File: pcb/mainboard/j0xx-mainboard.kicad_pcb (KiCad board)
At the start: 2 copper layers, 148 x 142 mm, 21 parts, among them J1 USB_C_Receptacle, Q1 BSS138, SW1 reset, U1 ATmega32U4-AU, Y1 Resonator

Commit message: wip
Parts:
- removed G***: LOGO, Outlines:pentagon
- added C7: 0.1u, Capacitor_SMD:C_0805_2012Metric, F.Cu at (237.4, 71.8)
- moved R5 43.6 mm to (240.2, 75.0), turned to 270 degrees
- moved C5 42.2 mm to (239.7, 82.2), turned to 270 degrees
- moved Y1 35.3 mm to (233.6, 88.1), turned to 180 degrees
- moved U1 34.1 mm to (234.0, 78.9), turned to 0 degrees
- moved C6 31.8 mm to (231.0, 72.6), turned to 0 degrees
- moved R7 29.2 mm to (228.5, 89.2), turned to 135 degrees
- moved SW1 27.0 mm to (226.3, 90.0), turned to 315 degrees
- moved C4 21.8 mm to (227.6, 75.3), turned to 90 degrees
- moved C3 19.0 mm to (223.2, 78.5), turned to 90 degrees
- moved C2 16.1 mm to (221.1, 78.5), turned to 90 degrees
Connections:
- J1 pad A10: (no net) -> Net-(J1-PadA10)
- J1 pad A3: (no net) -> Net-(J1-PadA3)
- J1 pad A8: (no net) -> Net-(J1-PadA8)
- J1 pad B10: (no net) -> Net-(J1-PadB10)
- J1 pad B3: (no net) -> Net-(J1-PadB3)
- J1 pad B8: (no net) -> Net-(J1-PadB8)
- U1 pad 1: (no net) -> BTN_MS
- U1 pad 10: (no net) -> BTN_LEFT
- U1 pad 11: (no net) -> BTN_DOWN
- U1 pad 12: (no net) -> BTN_RIGHT
- U1 pad 18: (no net) -> BTN_MODX
- U1 pad 19: (no net) -> BTN_MODY
- U1 pad 20: (no net) -> BTN_START
- U1 pad 21: (no net) -> Net-(U1-Pad21)
- U1 pad 22: (no net) -> Net-(U1-Pad22)
- U1 pad 25: (no net) -> Net-(U1-Pad25)
- U1 pad 26: (no net) -> Net-(U1-Pad26)
- U1 pad 27: (no net) -> BTN_CL
- U1 pad 28: (no net) -> BTN_CU
- U1 pad 29: (no net) -> BTN_CD
- U1 pad 30: (no net) -> BTN_A
- U1 pad 31: (no net) -> BTN_CR
- U1 pad 32: (no net) -> BTN_B
- U1 pad 36: (no net) -> BTN_X
- U1 pad 37: (no net) -> BTN_Z
- U1 pad 38: (no net) -> BTN_UP
- U1 pad 39: (no net) -> BTN_R
- U1 pad 40: (no net) -> BTN_Y
- U1 pad 41: (no net) -> BTN_LS
- U1 pad 42: (no net) -> Net-(U1-Pad42)
- U1 pad 9: (no net) -> BTN_L
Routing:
- net (no net): track 205.3 -> 0.00 mm
- net +5V: track 150.2 -> 128.2 mm
- net BTN_L: track 0.00 -> 16.4 mm
- net BTN_LEFT: track 0.00 -> 15.4 mm
- net BTN_DOWN: track 0.00 -> 14.5 mm
- net BTN_START: track 0.00 -> 14.2 mm
- net BTN_RIGHT: track 0.00 -> 13.4 mm
- net Net-(R3-Pad1): track 24.9 -> 37.4 mm
- net Net-(R4-Pad1): track 24.3 -> 36.0 mm
- net BTN_UP: track 0.00 -> 11.5 mm
- net BTN_Z: track 0.00 -> 11.3 mm
- net BTN_X: track 0.00 -> 11.1 mm
- net GND: track 74.3 -> 64.6 mm, vias 11 -> 9
- net GCCD5v: track 39.5 -> 47.2 mm
- net BTN_R: track 0.00 -> 7.08 mm
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- added copper zone on B.Cu, net GND
- added copper zone on F.Cu, net GND
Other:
- board size 148 x 142 mm -> 136.8 x 59.1 mm

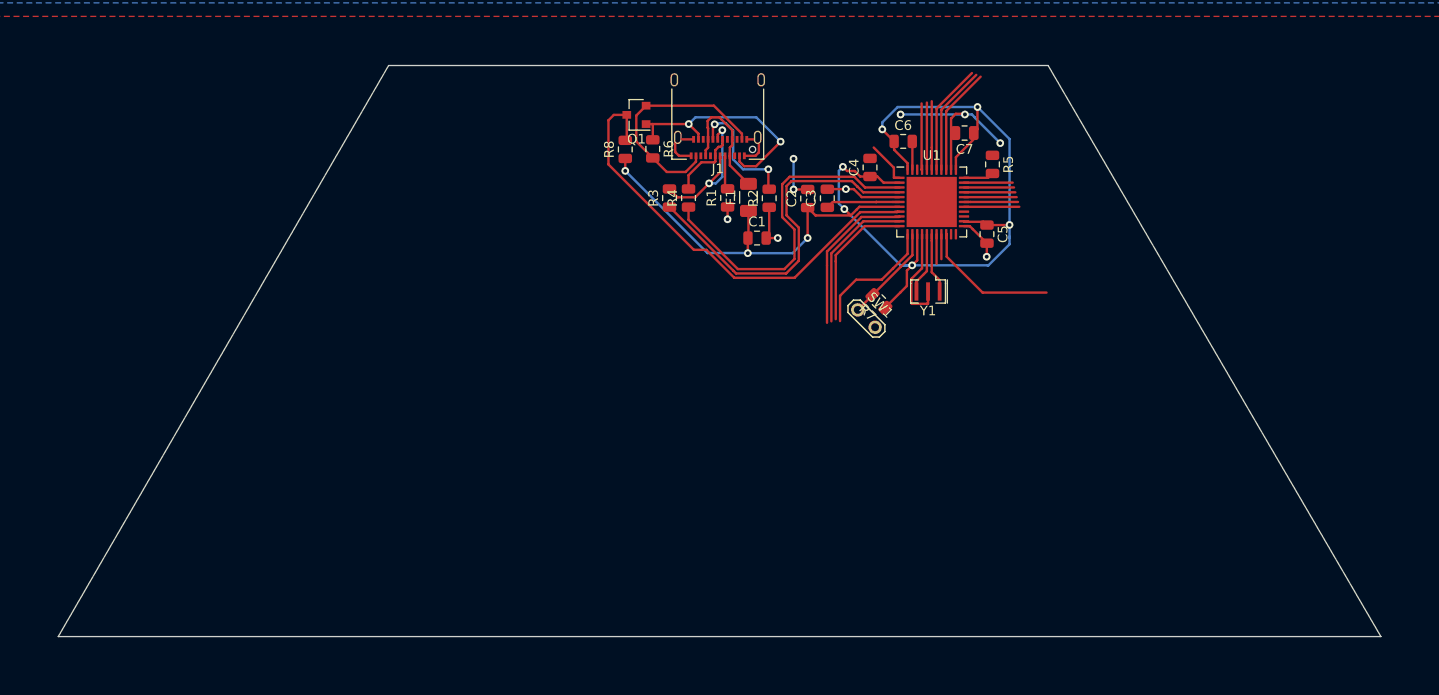
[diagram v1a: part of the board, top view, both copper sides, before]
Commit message: rearrange parts, add connectors and outline
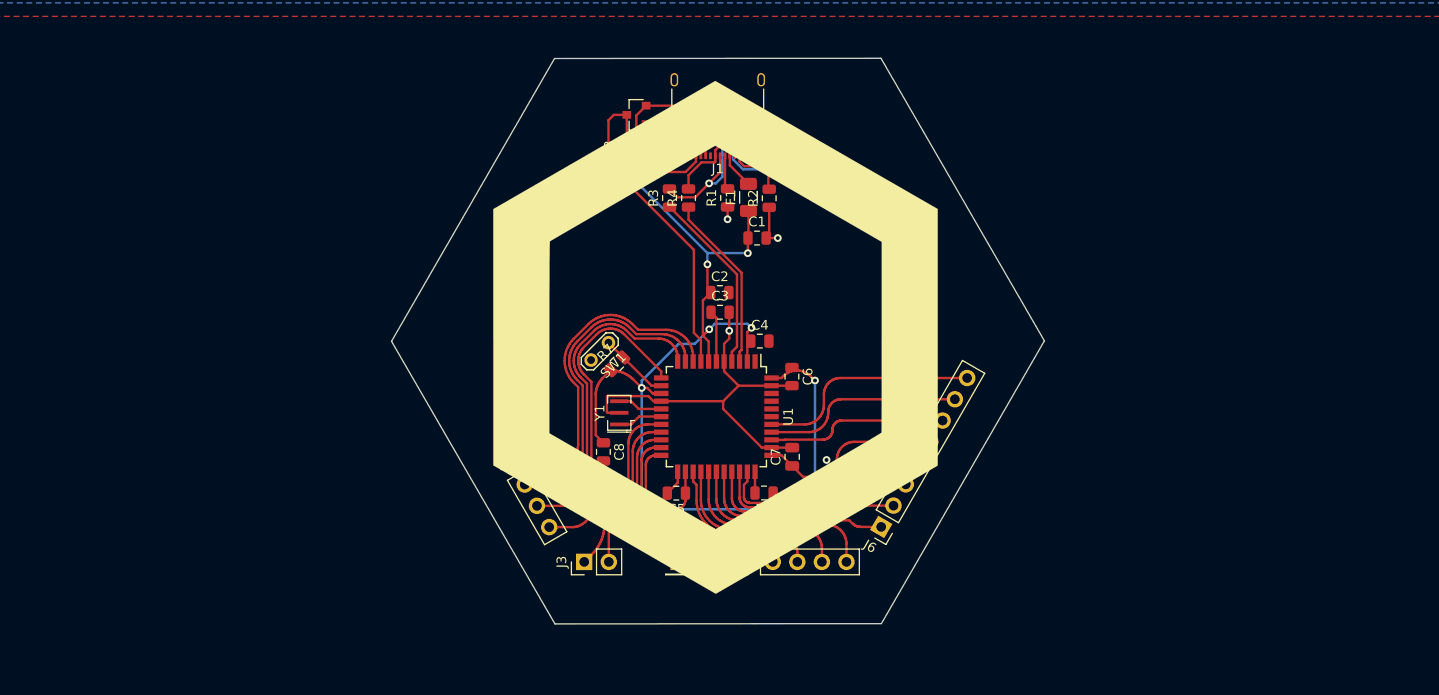
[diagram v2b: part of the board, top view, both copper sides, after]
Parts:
- added C8: 0.1u, Capacitor_SMD:C_0805_2012Metric, F.Cu at (200.0, 104.7)
- added G***: LOGO, Outlines:shine, F.Cu at (211.8, 92.8)
- added G***: LOGO, Outlines:shine, B.Cu at (211.8, 92.8)
- added J2: Conn_01x04, Connector_PinHeader_2.54mm:PinHeader_1x04_P2.54mm_Vertical, F.Cu at (190.6, 105.9)
- added J3: Conn_01x02, Connector_PinHeader_2.54mm:PinHeader_1x02_P2.54mm_Vertical, F.Cu at (198.0, 116.1)
- added J4: Conn_01x01, Connector_PinHeader_2.54mm:PinHeader_1x01_P2.54mm_Vertical, F.Cu at (207.8, 116.1)
- added J5: Conn_01x05, Connector_PinHeader_2.54mm:PinHeader_1x05_P2.54mm_Vertical, F.Cu at (215.0, 116.1)
- added J6: Conn_01x08, Connector_PinHeader_2.54mm:PinHeader_1x08_P2.54mm_Vertical, F.Cu at (228.7, 112.5)
- U1: footprint Package_DFN_QFN:QFN-44-1EP_7x7mm_P0.5mm_EP5.2x5.2mm -> Package_QFP:TQFP-44_10x10mm_P0.8mm
- moved C5 41.8 mm to (207.6, 109.0), turned to 180 degrees
- moved R5 41.4 mm to (216.6, 109.0), turned to 180 degrees
- moved C7 37.9 mm to (219.5, 105.2), turned to 90 degrees
- moved Y1 34.3 mm to (201.7, 100.7), turned to 90 degrees
- moved U1 31.4 mm to (211.7, 101.1), turned to 270 degrees
- moved R7 27.9 mm to (201.4, 95.6), turned to 45 degrees
- moved C6 26.9 mm to (219.5, 96.9), turned to 270 degrees
- moved SW1 26.0 mm to (200.5, 93.4), turned to 225 degrees
- moved C4 21.3 mm to (216.2, 93.3), turned to 0 degrees
- moved C3 16.2 mm to (212.1, 90.3), turned to 0 degrees
- moved C2 13.3 mm to (212.1, 88.3), turned to 0 degrees
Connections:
- U1 pad 1: BTN_MS -> Net-(U1-Pad1)
- U1 pad 21: Net-(U1-Pad21) -> BTN_CL
- U1 pad 22: Net-(U1-Pad22) -> BTN_CU
- U1 pad 25: Net-(U1-Pad25) -> BTN_CD
- U1 pad 26: Net-(U1-Pad26) -> BTN_A
- U1 pad 27: BTN_CL -> BTN_CR
- U1 pad 28: BTN_CU -> BTN_B
- U1 pad 29: BTN_CD -> BTN_X
- U1 pad 30: BTN_A -> BTN_Z
- U1 pad 31: BTN_CR -> BTN_UP
- U1 pad 32: BTN_B -> BTN_R
- U1 pad 36: BTN_X -> BTN_Y
- U1 pad 37: BTN_Z -> BTN_LS
- U1 pad 38: BTN_UP -> BTN_MS
- U1 pad 39: BTN_R -> Net-(U1-Pad39)
- U1 pad 40: BTN_Y -> Net-(U1-Pad40)
- U1 pad 41: BTN_LS -> Net-(U1-Pad41)
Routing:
- net BTN_RIGHT: track 13.4 -> 33.9 mm
- net BTN_R: track 7.08 -> 27.5 mm
- net BTN_DOWN: track 14.5 -> 34.5 mm
- net BTN_LEFT: track 15.4 -> 34.9 mm
- net BTN_L: track 16.4 -> 35.3 mm
- net BTN_MS: track 4.57 -> 23.4 mm
- net Net-(R3-Pad1): track 37.4 -> 19.1 mm
- net BTN_CU: track 5.58 -> 23.6 mm
- net Net-(R4-Pad1): track 36.0 -> 18.4 mm
- net BTN_CL: track 5.72 -> 22.4 mm
- net BTN_CR: track 5.17 -> 21.6 mm
- net BTN_B: track 5.04 -> 21.4 mm
- net BTN_MODX: track 3.06 -> 19.0 mm
- net BTN_MODY: track 2.57 -> 17.0 mm
- net BTN_A: track 5.31 -> 19.7 mm
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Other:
- board size 136.8 x 59.1 mm -> 67.5 x 58.5 mm

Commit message: wip
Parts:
- J2: value Conn_01x04 -> Conn_01x07; footprint Connector_PinHeader_2.54mm:PinHeader_1x04_P2.54mm_Vertical -> Connector_PinHeader_2.54mm:PinHeader_1x07_P2.54mm_Vertical
- J3: value Conn_01x02 -> Conn_01x05; footprint Connector_PinHeader_2.54mm:PinHeader_1x02_P2.54mm_Vertical -> Connector_PinHeader_2.54mm:PinHeader_1x05_P2.54mm_Vertical
- J4: value Conn_01x01 -> Conn_01x04; footprint Connector_PinHeader_2.54mm:PinHeader_1x01_P2.54mm_Vertical -> Connector_PinHeader_2.54mm:PinHeader_1x04_P2.54mm_Vertical
- J5: value Conn_01x05 -> Conn_01x08; footprint Connector_PinHeader_2.54mm:PinHeader_1x05_P2.54mm_Vertical -> Connector_PinHeader_2.54mm:PinHeader_1x08_P2.54mm_Vertical
- J6: value Conn_01x08 -> Conn_01x10; footprint Connector_PinHeader_2.54mm:PinHeader_1x08_P2.54mm_Vertical -> Connector_PinHeader_2.54mm:PinHeader_1x10_P2.54mm_Vertical
- moved J2 30.8 mm to (192.2, 75.2), turned to 330 degrees
- moved J6 24.6 mm to (240.7, 90.9), turned to 210 degrees
- moved J3 17.9 mm to (186.9, 102.1), turned to 30 degrees
- moved J5 15.1 mm to (229.9, 113.4), turned to 150 degrees
- moved J4 3.93 mm to (207.4, 120.0), turned to 90 degrees
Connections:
- J2 pad 1: BTN_L -> GND
- J2 pad 2: BTN_LEFT -> LED_DATA
- J2 pad 3: BTN_DOWN -> BTN_L
- J2 pad 4: BTN_RIGHT -> BTN_LEFT
- J3 pad 1: BTN_MODX -> GND
- J3 pad 2: BTN_MODY -> LED_1-2
- J4 pad 1: BTN_START -> GND
- J5 pad 1: BTN_CL -> GND
- J5 pad 2: BTN_CU -> LED_3-4
- J5 pad 3: BTN_CD -> BTN_CL
- J5 pad 4: BTN_A -> BTN_CU
- J5 pad 5: BTN_CR -> BTN_CD
- J6 pad 1: BTN_B -> GND
- J6 pad 2: BTN_X -> LED_4-5
- J6 pad 3: BTN_Z -> BTN_B
- J6 pad 4: BTN_UP -> BTN_X
- J6 pad 5: BTN_R -> BTN_Z
- J6 pad 6: BTN_Y -> BTN_UP
- J6 pad 7: BTN_LS -> BTN_R
- J6 pad 8: BTN_MS -> BTN_Y
- U1 pad 1: Net-(U1-Pad1) -> LED_DATA
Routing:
- net LED_DATA: track 0.00 -> 40.8 mm, vias 0 -> 2
- net LED_2-3: track 0.00 -> 30.0 mm
- net LED_3-4: track 0.00 -> 28.6 mm
- net BTN_B: track 21.4 -> 48.0 mm
- net BTN_X: track 21.8 -> 48.1 mm
- net LED_1-2: track 0.00 -> 25.4 mm
- net BTN_Z: track 23.3 -> 48.2 mm
- net BTN_UP: track 25.2 -> 48.3 mm
- net BTN_R: track 27.5 -> 48.9 mm
- net BTN_CL: track 22.4 -> 43.7 mm
- net BTN_CU: track 23.6 -> 44.8 mm
- net BTN_CD: track 17.6 -> 38.6 mm
- net BTN_A: track 19.7 -> 40.6 mm
- net BTN_CR: track 21.6 -> 42.4 mm
- net LED_4-5: track 0.00 -> 19.1 mm
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
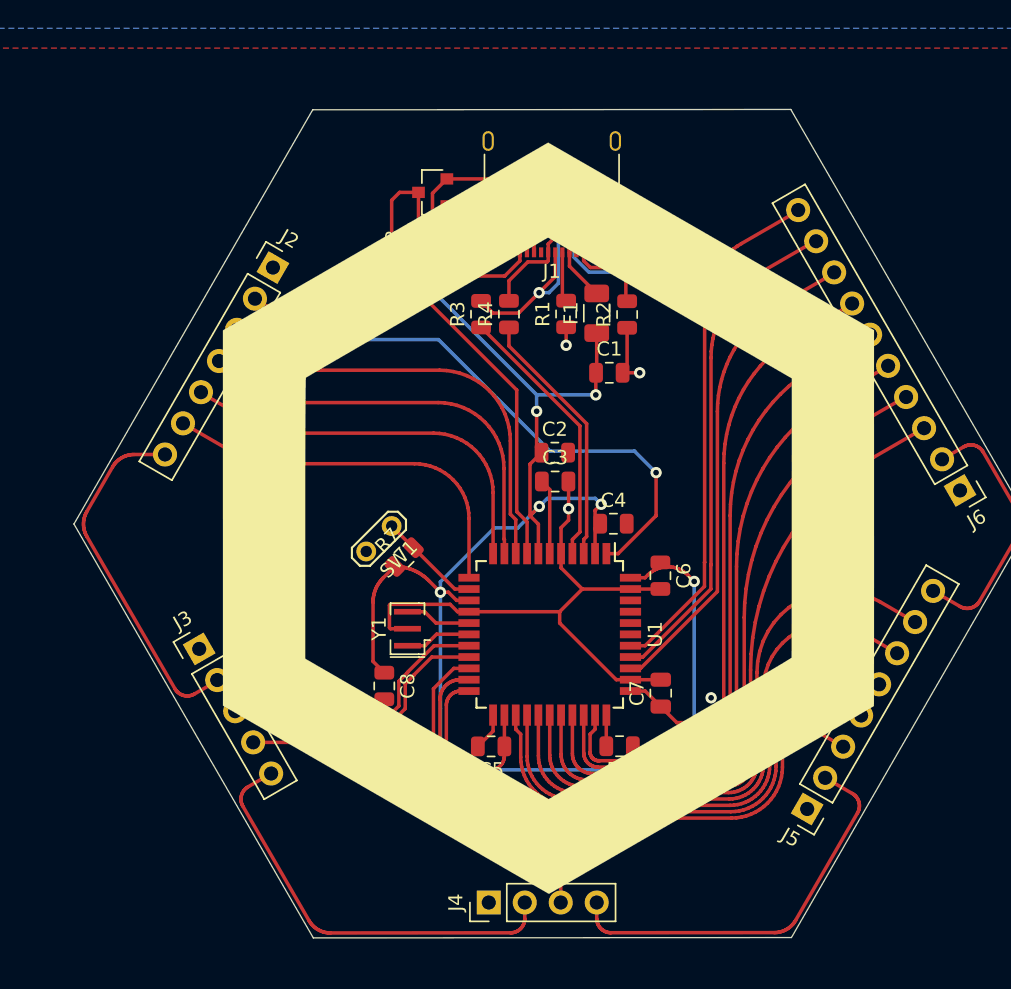
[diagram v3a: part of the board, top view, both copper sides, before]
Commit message: Protruding USB port, tilted MCU
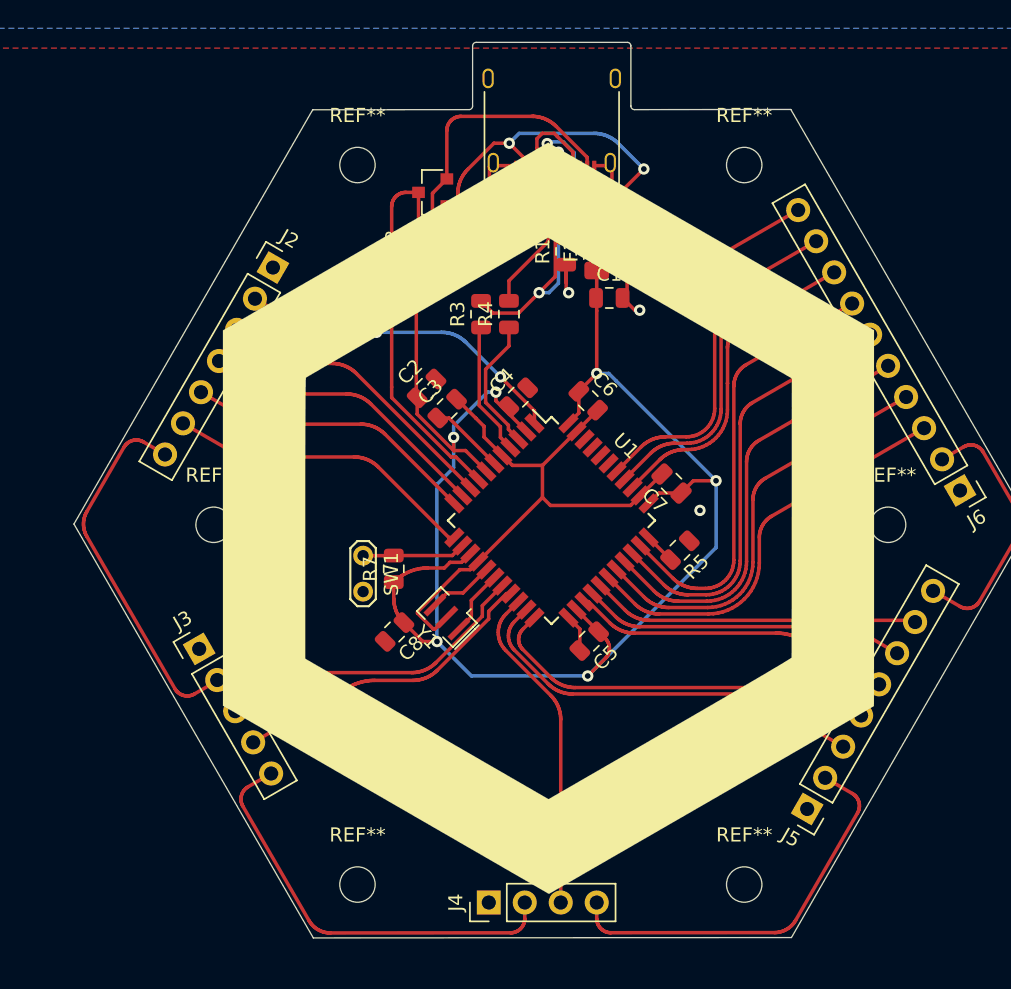
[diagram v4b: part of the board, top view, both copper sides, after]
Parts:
- added REF**: MountingHole_2.5mm, MountingHole:MountingHole_2.5mm, F.Cu at (235.6, 93.3)
- added REF**: MountingHole_2.5mm, MountingHole:MountingHole_2.5mm, F.Cu at (188.0, 93.3)
- added REF**: MountingHole_2.5mm, MountingHole:MountingHole_2.5mm, F.Cu at (225.4, 118.7)
- added REF**: MountingHole_2.5mm, MountingHole:MountingHole_2.5mm, F.Cu at (198.1, 118.7)
- added REF**: MountingHole_2.5mm, MountingHole:MountingHole_2.5mm, F.Cu at (225.4, 67.9)
- added REF**: MountingHole_2.5mm, MountingHole:MountingHole_2.5mm, F.Cu at (198.1, 67.9)
- moved C7 14.8 mm to (220.3, 90.4), turned to 135 degrees
- moved R5 14.5 mm to (220.9, 95.1), turned to 225 degrees
- moved C6 13.4 mm to (214.4, 84.6), turned to 315 degrees
- moved C4 11.2 mm to (209.5, 84.3), turned to 45 degrees
- moved C5 10.2 mm to (214.5, 101.6), turned to 225 degrees
- moved C2 10.1 mm to (203.0, 83.7), turned to 45 degrees
- moved C3 9.20 mm to (204.5, 85.1), turned to 45 degrees
- moved U1 8.04 mm to (211.8, 93.0), turned to 315 degrees
- moved C1 5.28 mm to (215.9, 77.3)
- moved F1 4.42 mm to (215.0, 74.0)
- moved R1 4.42 mm to (212.9, 74.0)
- moved R2 4.42 mm to (217.2, 74.1)
- moved J1 4.42 mm to (211.8, 64.7)
- moved C8 3.88 mm to (200.7, 100.9), turned to 225 degrees
- moved SW1 2.91 mm to (198.5, 95.5), turned to 270 degrees
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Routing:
- net BTN_CR: track 42.4 -> 22.9 mm
- net BTN_B: track 48.0 -> 29.7 mm
- net BTN_X: track 48.1 -> 30.2 mm
- net BTN_A: track 40.6 -> 22.8 mm
- net BTN_Z: track 48.2 -> 30.7 mm
- net LED_DATA: track 40.8 -> 23.4 mm
- net BTN_R: track 48.9 -> 31.6 mm
- net BTN_UP: track 48.3 -> 31.1 mm
- net BTN_CU: track 44.8 -> 28.1 mm
- net BTN_CD: track 38.6 -> 22.5 mm
- net BTN_CL: track 43.7 -> 28.8 mm
- net BTN_Y: track 34.7 -> 23.3 mm
- net BTN_LS: track 35.7 -> 24.7 mm
- net BTN_L: track 31.1 -> 20.6 mm
- net BTN_MS: track 36.7 -> 26.3 mm
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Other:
- board size 67.5 x 58.5 mm -> 67.5 x 63.2 mm
